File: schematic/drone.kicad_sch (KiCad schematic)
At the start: 35 parts, among them J1 Conn_01x04_Pin, J2 USB_B_Micro, J3 Conn_01x04_Pin, J4 Conn_01x04_Pin, SW1 SW_SPDT, U1 MPU-6000, U3 NCP1117-3.3_SOT223, U4 STM32F427VITx, Y2 16MHz

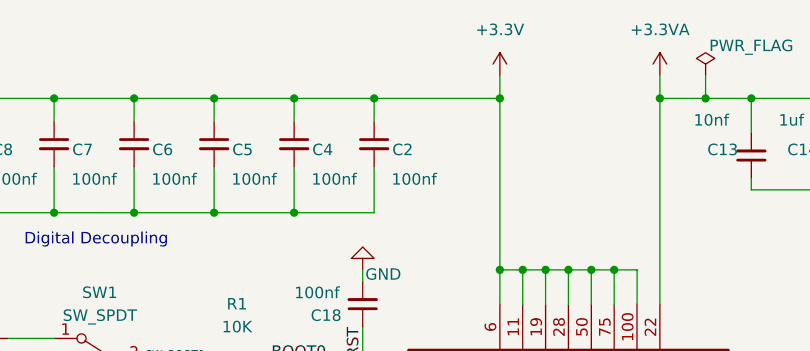
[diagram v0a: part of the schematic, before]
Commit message: fixing ERC errors
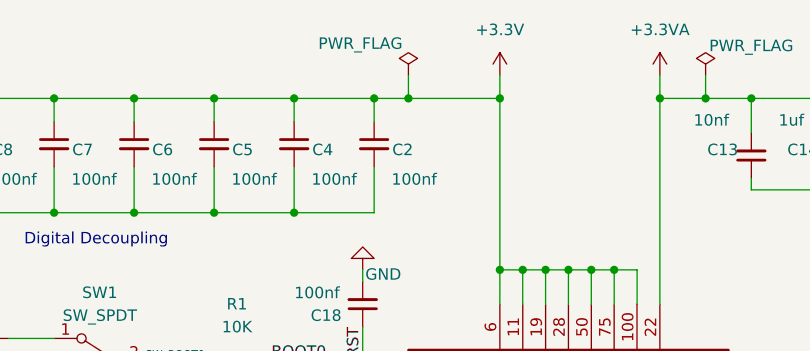
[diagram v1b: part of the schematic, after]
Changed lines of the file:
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@@
 	)
 	(junction
+		(at 184.15 73.66)
+		(diameter 0)
+		(color 0 0 0 0)
+	)
+	(junction
 		(at 135.89 86.36)
 		(diameter 0)
@@
 	(wire
 		(pts
+			(xy 184.15 71.12) (xy 184.15 73.66)
+		)
+		(stroke
+			(width 0)
+			(type default)
+		)
+	)
+	(wire
+		(pts
 			(xy 240.03 149.86) (xy 243.84 149.86)
 		)
@@
 	(wire
 		(pts
+			(xy 184.15 73.66) (xy 194.31 73.66)
+		)
+		(stroke
+			(width 0)
+			(type default)
+		)
+	)
+	(wire
+		(pts
 			(xy 247.65 73.66) (xy 247.65 77.47)
 		)
@@
 	(wire
 		(pts
-			(xy 180.34 73.66) (xy 194.31 73.66)
+			(xy 180.34 73.66) (xy 184.15 73.66)
 		)
 		(stroke
@@
 					(unit 1)
 				)
+			)
+		)
+	)
+	(symbol
+		(lib_id "power:PWR_FLAG")
+		(at 184.15 71.12 0)
+		(unit 1)
+		(exclude_from_sim no)
+		(in_bom yes)
+		(on_board yes)
+		(dnp no)
+		(property "Reference" "#FLG02"
+			(at 184.15 69.215 0)
+			(effects
+				(font
+					(size 1.27 1.27)
+				)
+				(hide yes)
+			)
+		)
+		(property "Value" "PWR_FLAG"
+			(at 178.816 67.564 0)
+			(effects
+				(font
+					(size 1.27 1.27)
+				)
+			)
+		)
+		(property "Footprint" ""
+			(at 184.15 71.12 0)
+			(effects
+				(font
+					(size 1.27 1.27)
+				)
+				(hide yes)
+			)
+		)
+		(property "Datasheet" "~"
+			(at 184.15 71.12 0)
+			(effects
+				(font
+					(size 1.27 1.27)
+				)
+				(hide yes)
+			)
+		)
+		(property "Description" "Special symbol for telling ERC where power comes from"
+			(at 184.15 71.12 0)
+			(effects
+				(font
+					(size 1.27 1.27)
+				)
+				(hide yes)
+			)
+		)
+		(pin "1"
+		)
+		(instances
+			(project "drone"
+				(path "/bfc8e452-ea96-4fb3-a8d4-30d5739a61c9"
+					(reference "#FLG02")
+					(unit 1)
+				)

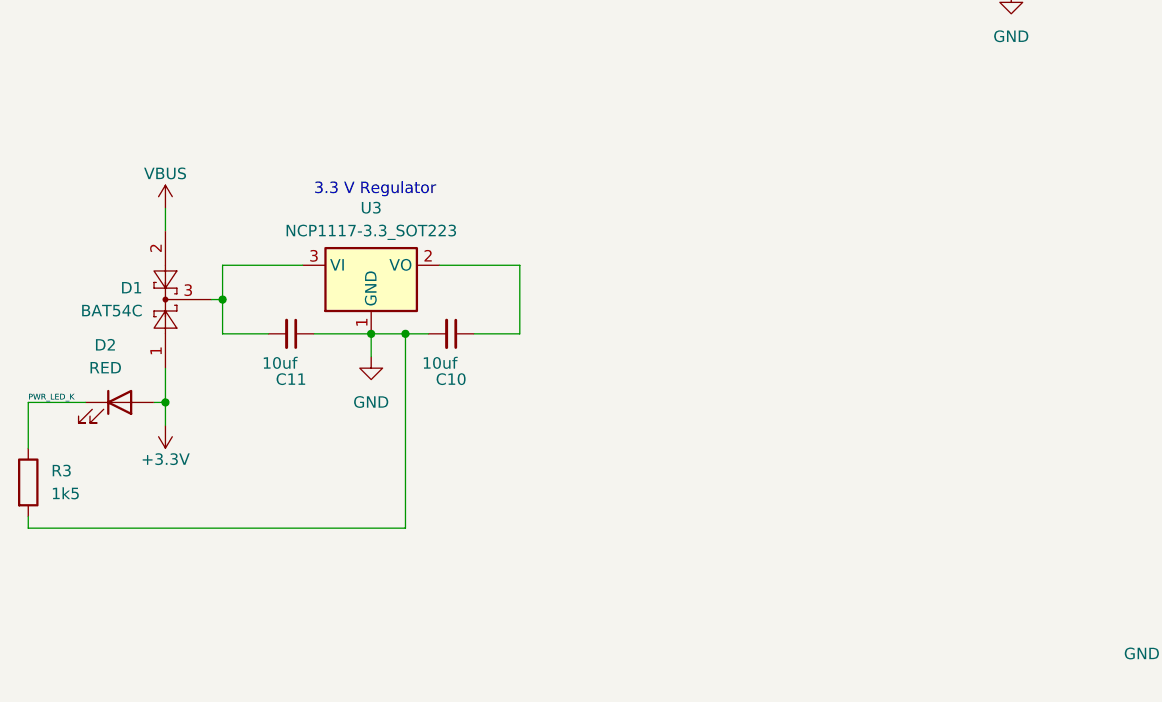
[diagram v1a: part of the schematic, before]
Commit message: adding power flag to regulator
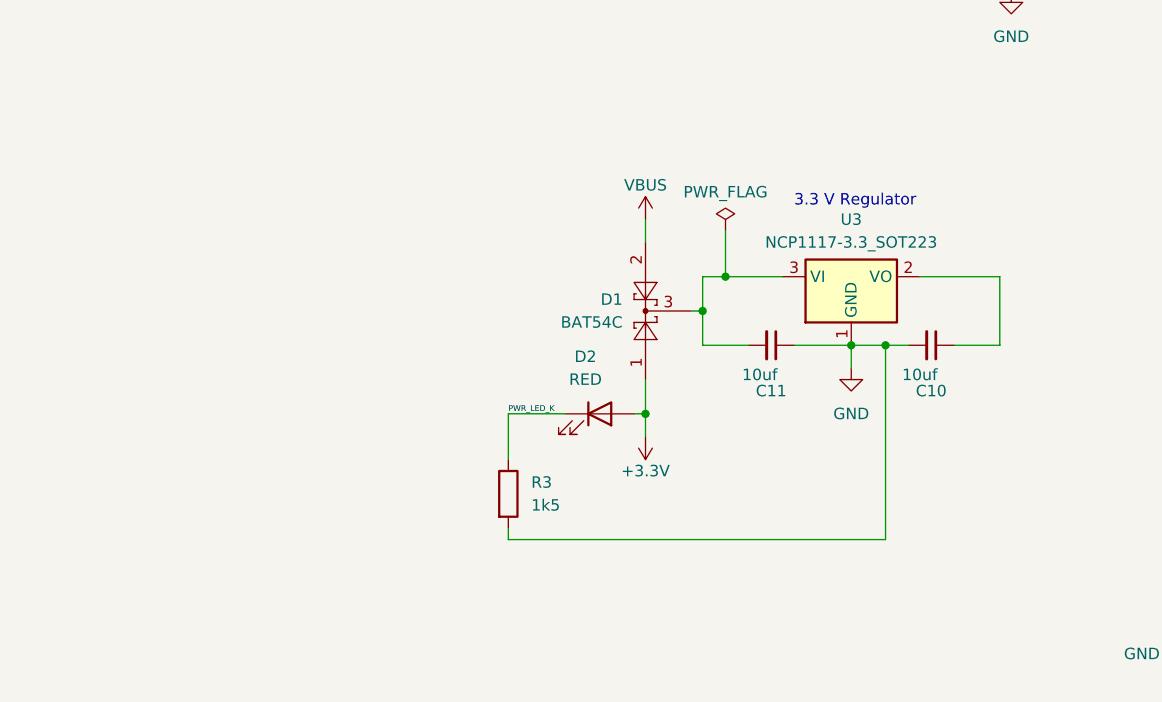
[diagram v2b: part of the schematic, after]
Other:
- moved on the sheet: C10, C11, D1, D2, R3, U3

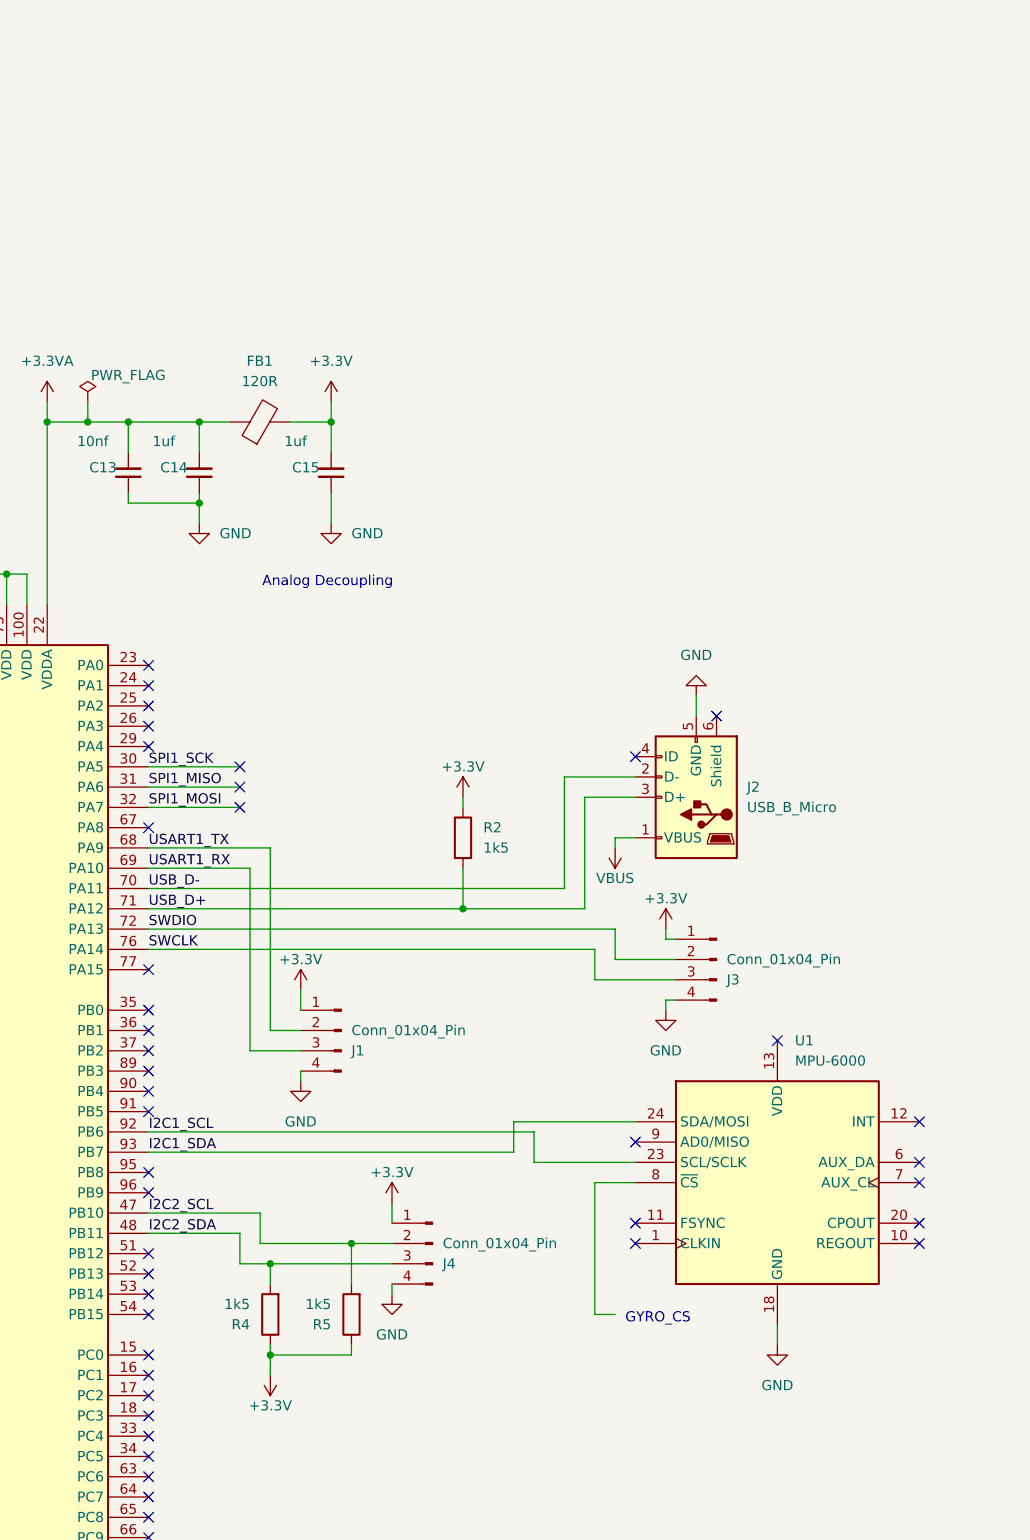
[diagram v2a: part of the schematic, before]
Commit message: wiring MPU-6000 gyro
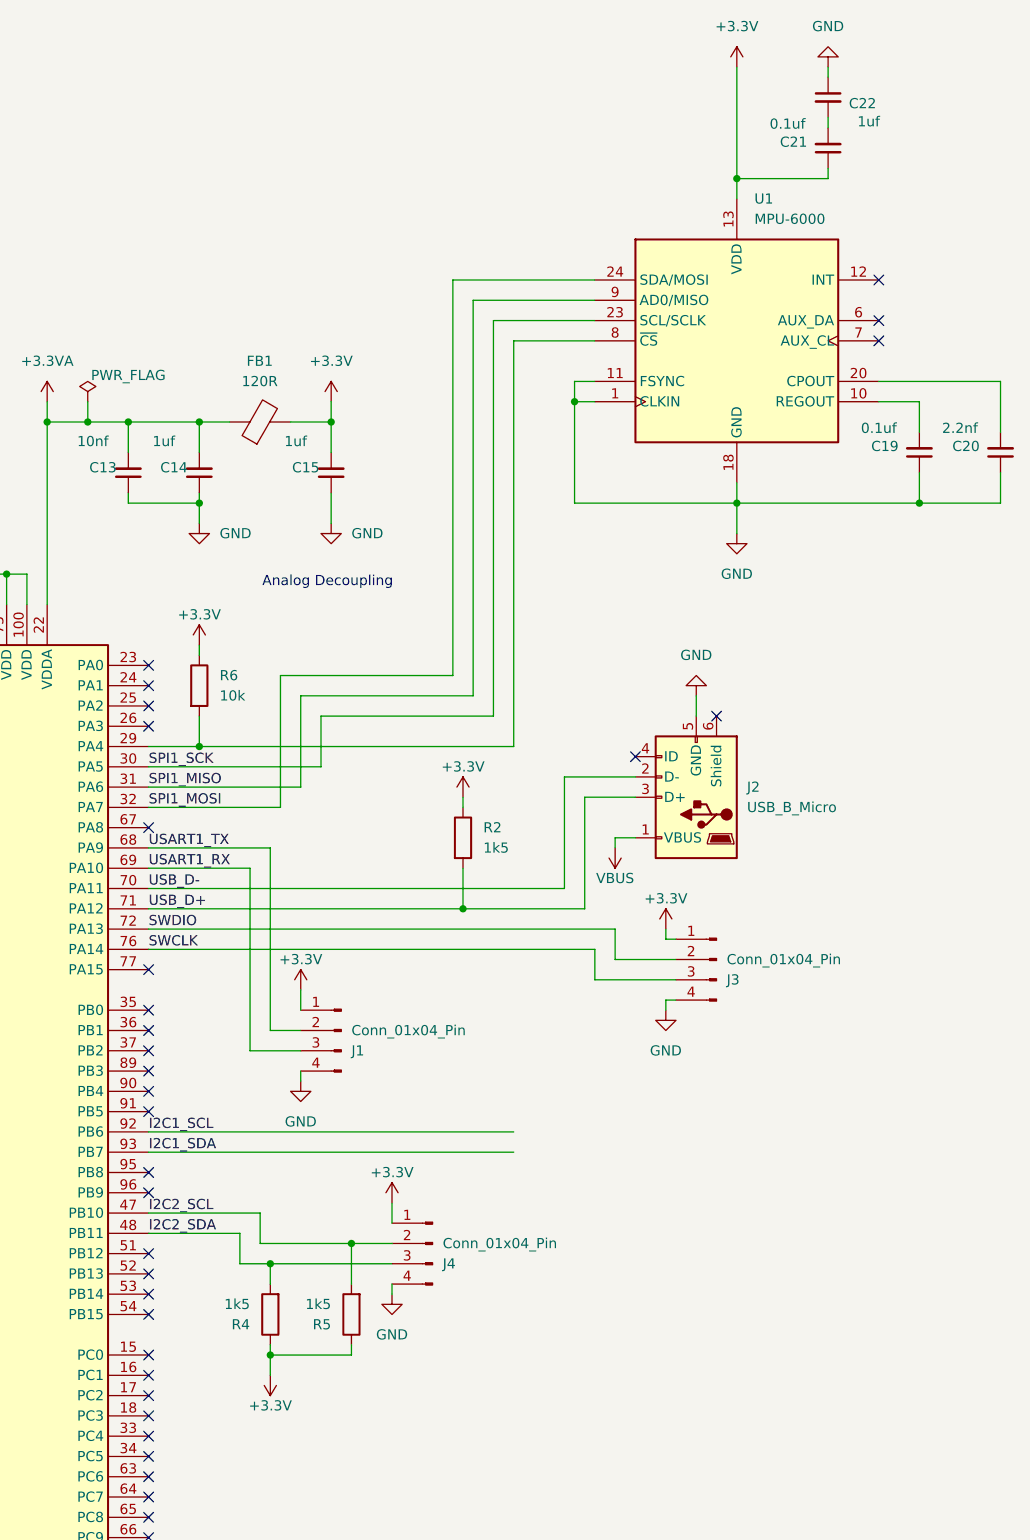
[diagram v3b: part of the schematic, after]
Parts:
- added C19, C21: 0.1uf, symbol Device:C_Small
- added C20: 2.2nf, symbol Device:C_Small
- added C22: 1uf, symbol Device:C_Small
- added R6: 10k, symbol Device:R
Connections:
- net +3.3V: now also U1.13 (VDD), C21.1, R6.1
- net GND: now also U1.1 (CLKIN), U1.11 (FSYNC), C19.1, C20.1, C22.1
- net I2C1_SCL: no longer U1.23 (SCL/SCLK)
- net I2C1_SDA: no longer U1.24 (SDA/MOSI)
- net SPI1_MISO: now also U1.9 (AD0/MISO)
- net SPI1_MOSI: now also U1.24 (SDA/MOSI)
- net SPI1_SCK: now also U1.23 (SCL/SCLK)
- net at U1.10 (REGOUT): now also C19.2
- net at U1.20 (CPOUT): now also C20.2
- net at U1.8 (~{CS}): now also U4.29 (PA4), R6.2
- new net: C21.2, C22.2
- no-connect marks 82 -> 72
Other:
- note removed: "GYRO_CS"
- moved on the sheet: U1

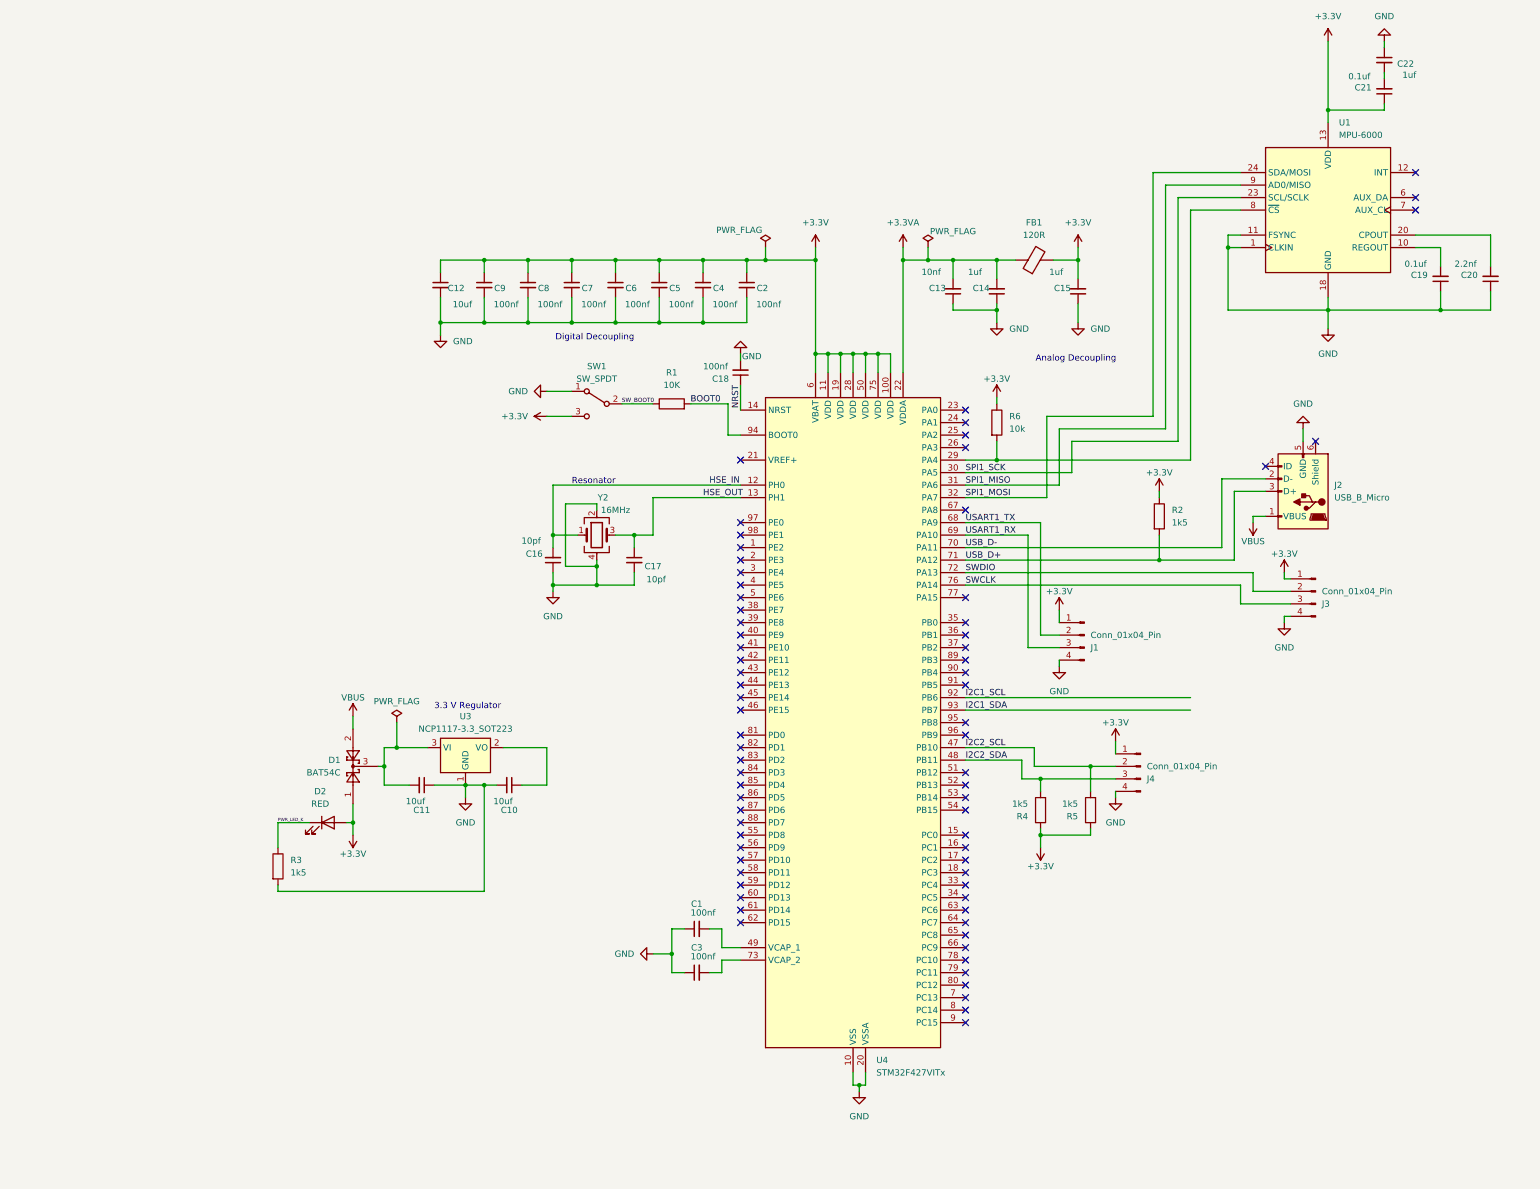
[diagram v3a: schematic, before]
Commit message: adding and wiring barometer
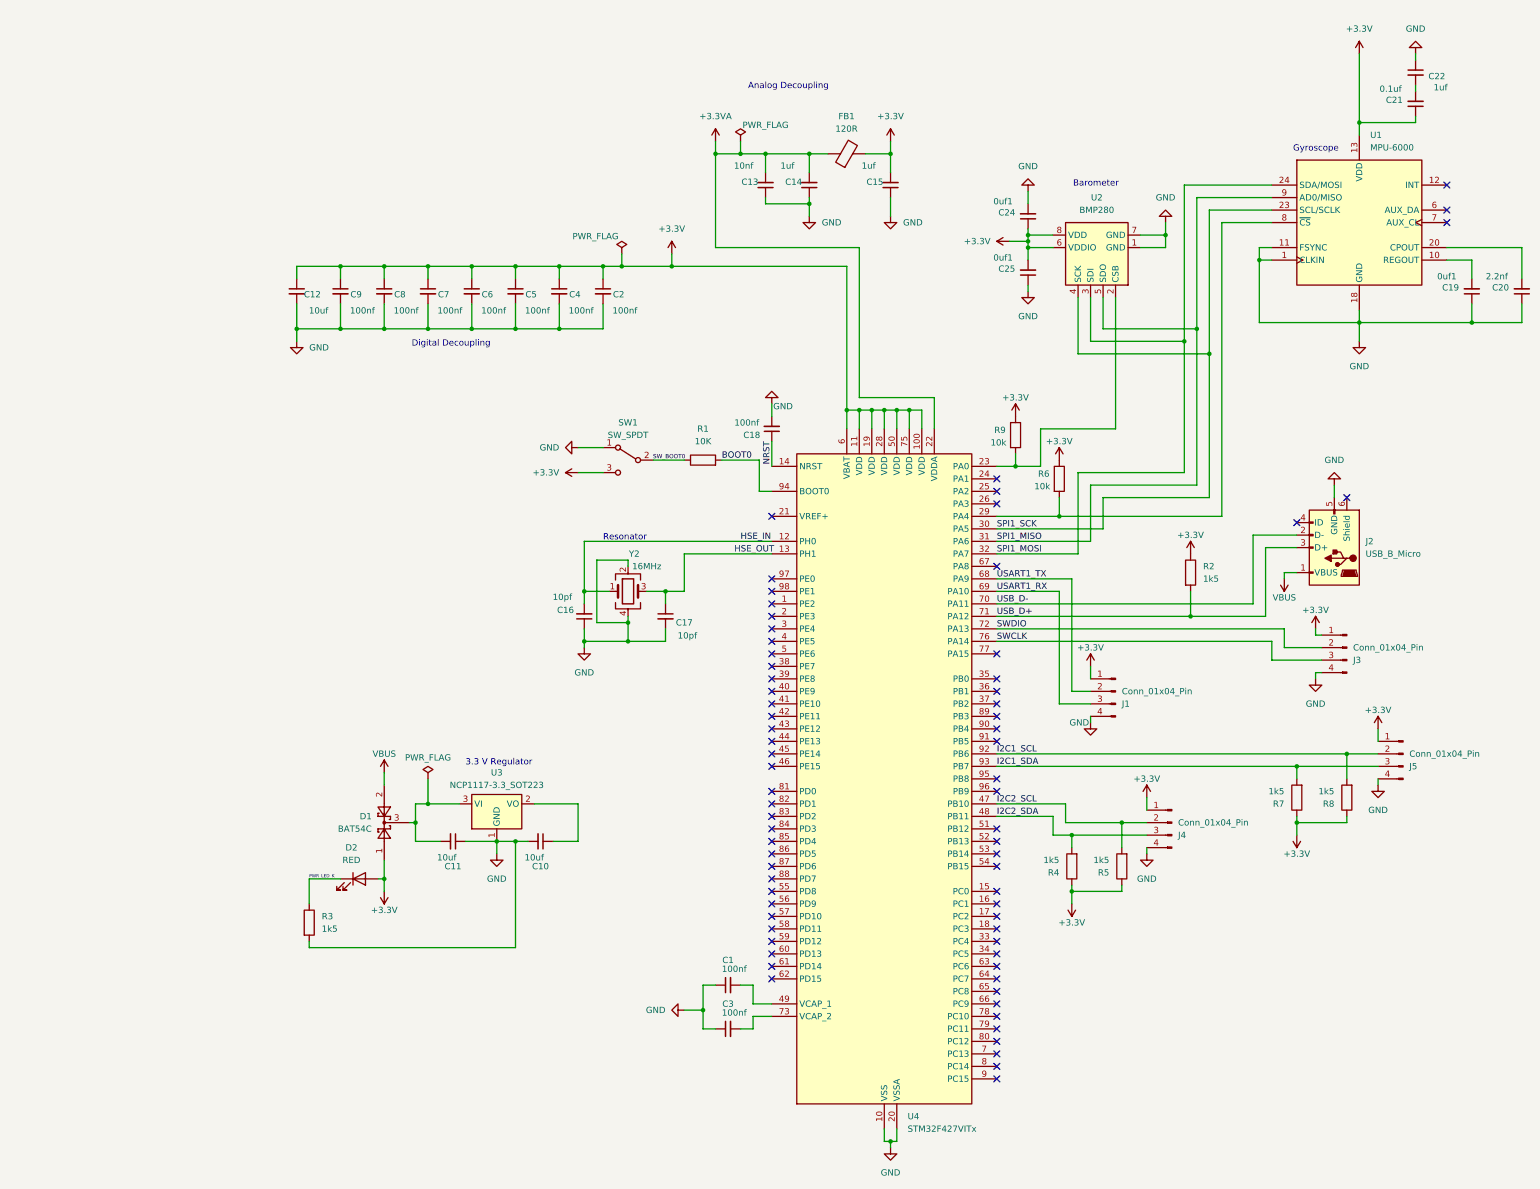
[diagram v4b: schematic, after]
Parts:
- added C24, C25: 0uf1, symbol Device:C_Small
- added J5: Conn_01x04_Pin, symbol Connector:Conn_01x04_Pin
- added R7, R8: 1k5, symbol Device:R
- added R9: 10k, symbol Device:R
- added U2: BMP280, Package_LGA:Bosch_LGA-8_2x2.5mm_P0.65mm_ClockwisePinNumbering, symbol Sensor_Pressure:BMP280
- C19: value 0.1uf -> 0uf1
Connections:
- net +3.3V: now also C24.1, C25.2, J5.1 (Pin_1), R7.1, R8.1, R9.1, U2.6 (VDDIO), U2.8 (VDD)
- net GND: now also C24.2, C25.1, J5.4 (Pin_4), U2.1 (GND), U2.7 (GND)
- net I2C1_SCL: now also J5.2 (Pin_2), R8.2
- net I2C1_SDA: now also J5.3 (Pin_3), R7.2
- net SPI1_MISO: now also U2.5 (SDO)
- net SPI1_MOSI: now also U2.3 (SDI)
- net SPI1_SCK: now also U2.4 (SCK)
- net at U4.23 (PA0): now also R9.2, U2.2 (CSB)
- no-connect marks 72 -> 71
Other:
- note added: "Barometer"
- note added: "Gyroscope"
- company: (none) -> Ozair Khan
- moved on the sheet: C1, C10, C11, C12, C13, C14, C15, C16, C17, C18, C19, C2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
